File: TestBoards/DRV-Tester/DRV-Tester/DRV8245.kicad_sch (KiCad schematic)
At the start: 2 parts, among them IC1 DRV8245SQRXZRQ1, U1 PDRV8245HRXZQ1

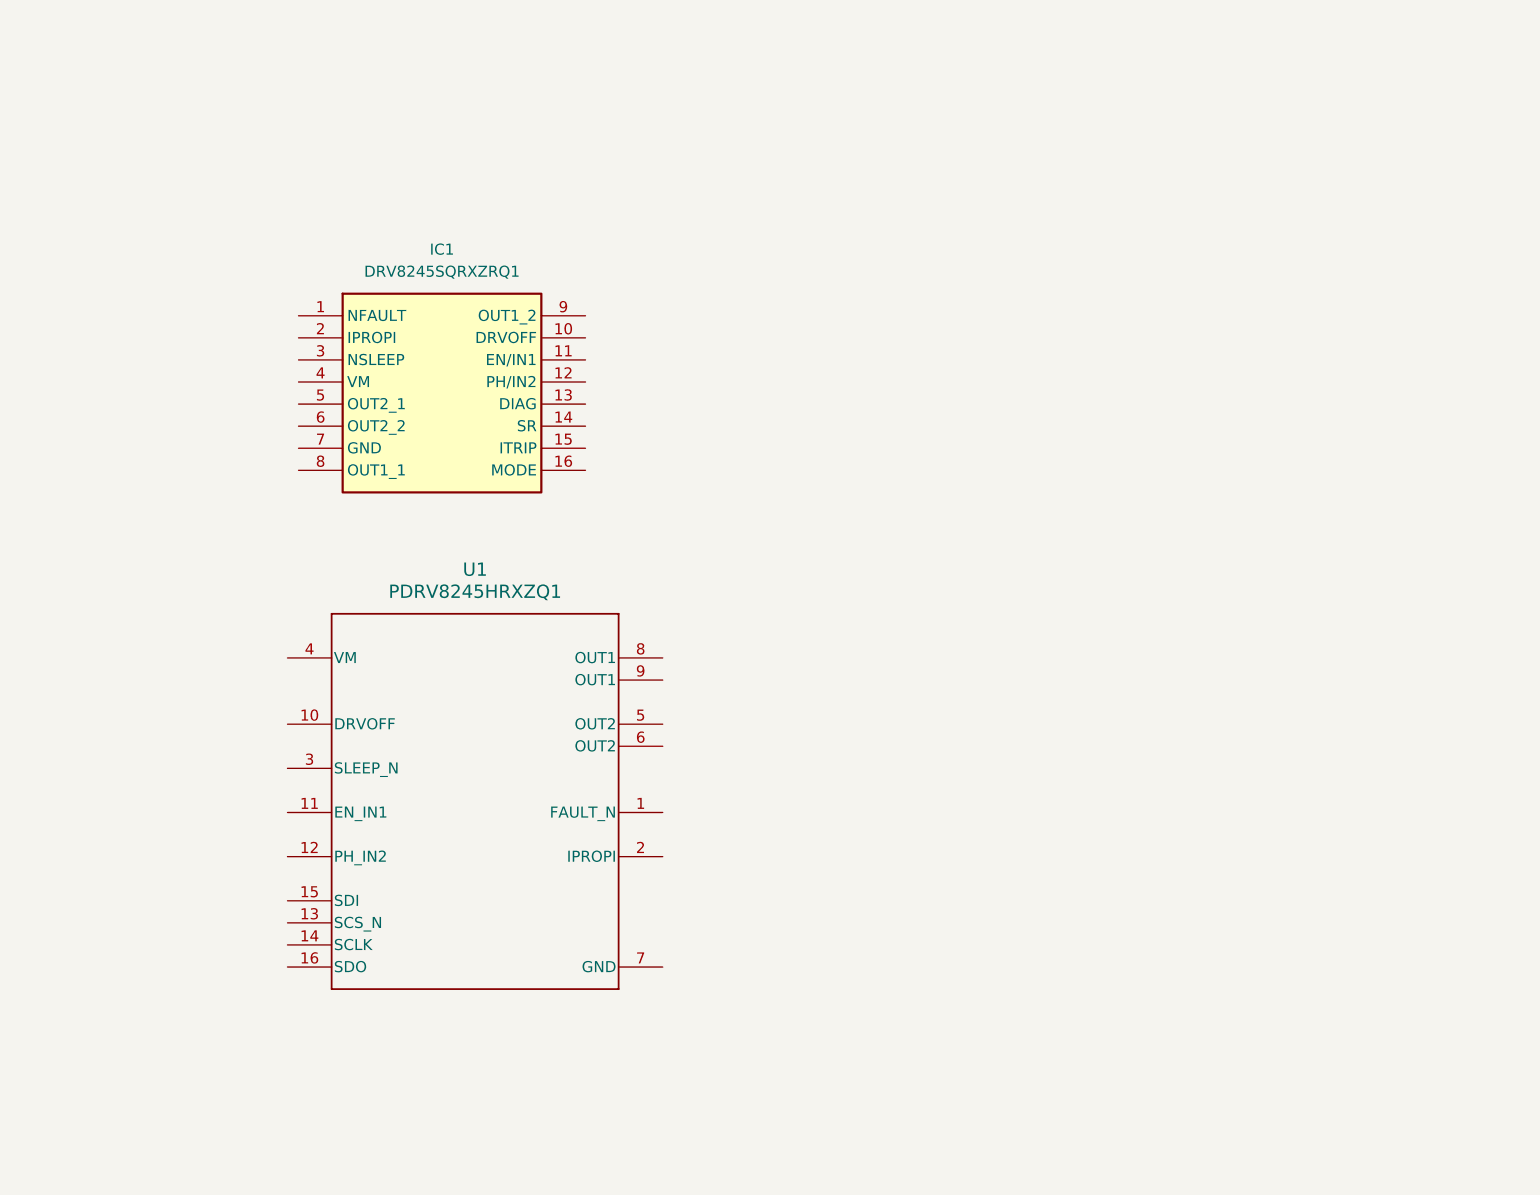
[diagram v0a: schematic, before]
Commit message: update new tester board sch
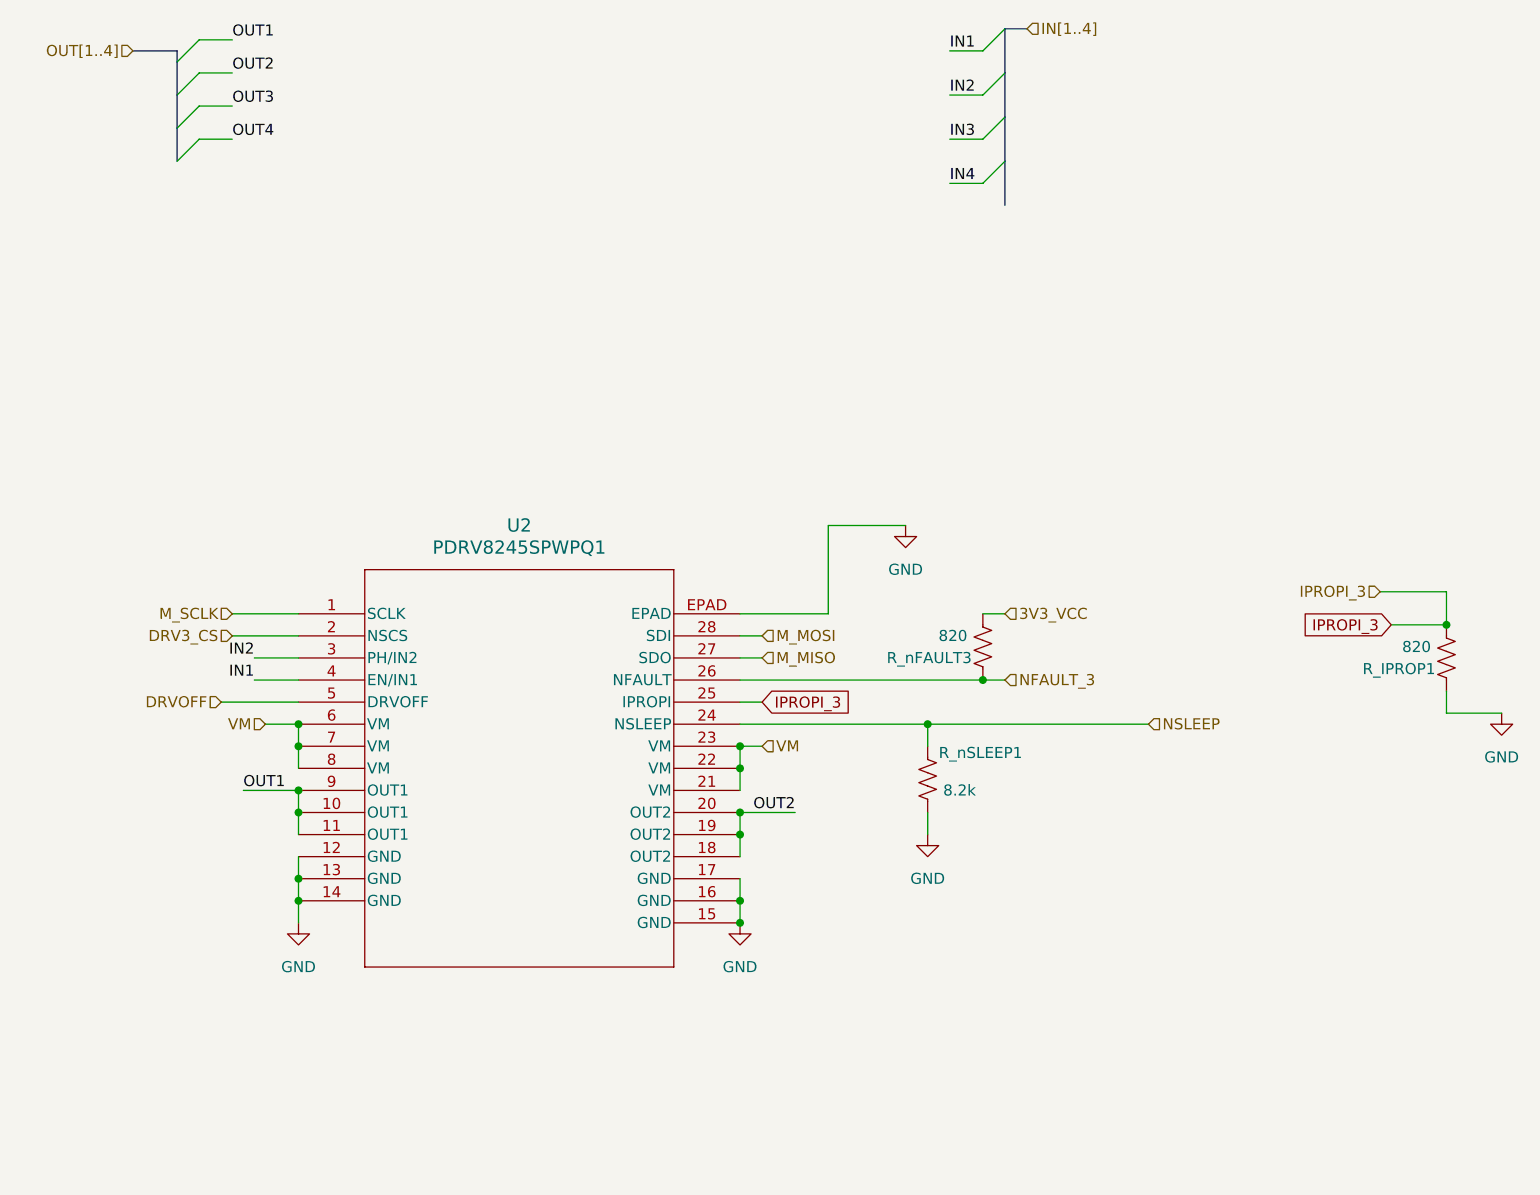
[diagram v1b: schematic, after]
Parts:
- removed IC1: DRV8245SQRXZRQ1, SamacSys_Parts:DRV8245HQRXZRQ1, symbol SamacSys_Parts:DRV8245SQRXZRQ1
- removed U1: PDRV8245HRXZQ1, PDRV8245SPWPQ1:U_PWP0028R_TEX, symbol PDRV8245HRXZQ1:PDRV8245HRXZQ1
- added R_IPROP1, R_nFAULT3: 820, Resistor_SMD:R_0603_1608Metric, symbol Device:R_US
- added R_nSLEEP1: 8.2k, Resistor_SMD:R_0603_1608Metric, symbol Device:R_US
- added U2: PDRV8245SPWPQ1, U_PWP0028R_TEX, symbol PDRV8245SPWPQ1:PDRV8245SPWPQ1
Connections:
- new net 3V3_VCC: R_nFAULT3.1
- new net DRV3_CS: U2.2 (NSCS)
- new net DRVOFF: U2.5 (DRVOFF)
- new net GND: R_IPROP1.2, R_nSLEEP1.1, U2.12 (GND), U2.13 (GND), U2.14 (GND), U2.15 (GND), U2.16 (GND), U2.17 (GND), U2.EPAD
- new net IN1: U2.4 (EN/IN1)
- new net IN2: U2.3 (PH/IN2)
- new net IPROPI_3: R_IPROP1.1, U2.25 (IPROPI)
- new net M_MISO: U2.27 (SDO)
- new net M_MOSI: U2.28 (SDI)
- new net M_SCLK: U2.1 (SCLK)
- new net NFAULT_3: R_nFAULT3.2, U2.26 (NFAULT)
- new net NSLEEP: R_nSLEEP1.2, U2.24 (NSLEEP)
- new net OUT1: U2.10 (OUT1), U2.11 (OUT1), U2.9 (OUT1)
- new net OUT2: U2.18 (OUT2), U2.19 (OUT2), U2.20 (OUT2)
- new net VM: U2.21 (VM), U2.22 (VM), U2.23 (VM), U2.6 (VM), U2.7 (VM), U2.8 (VM)

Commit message: update tester board with layout
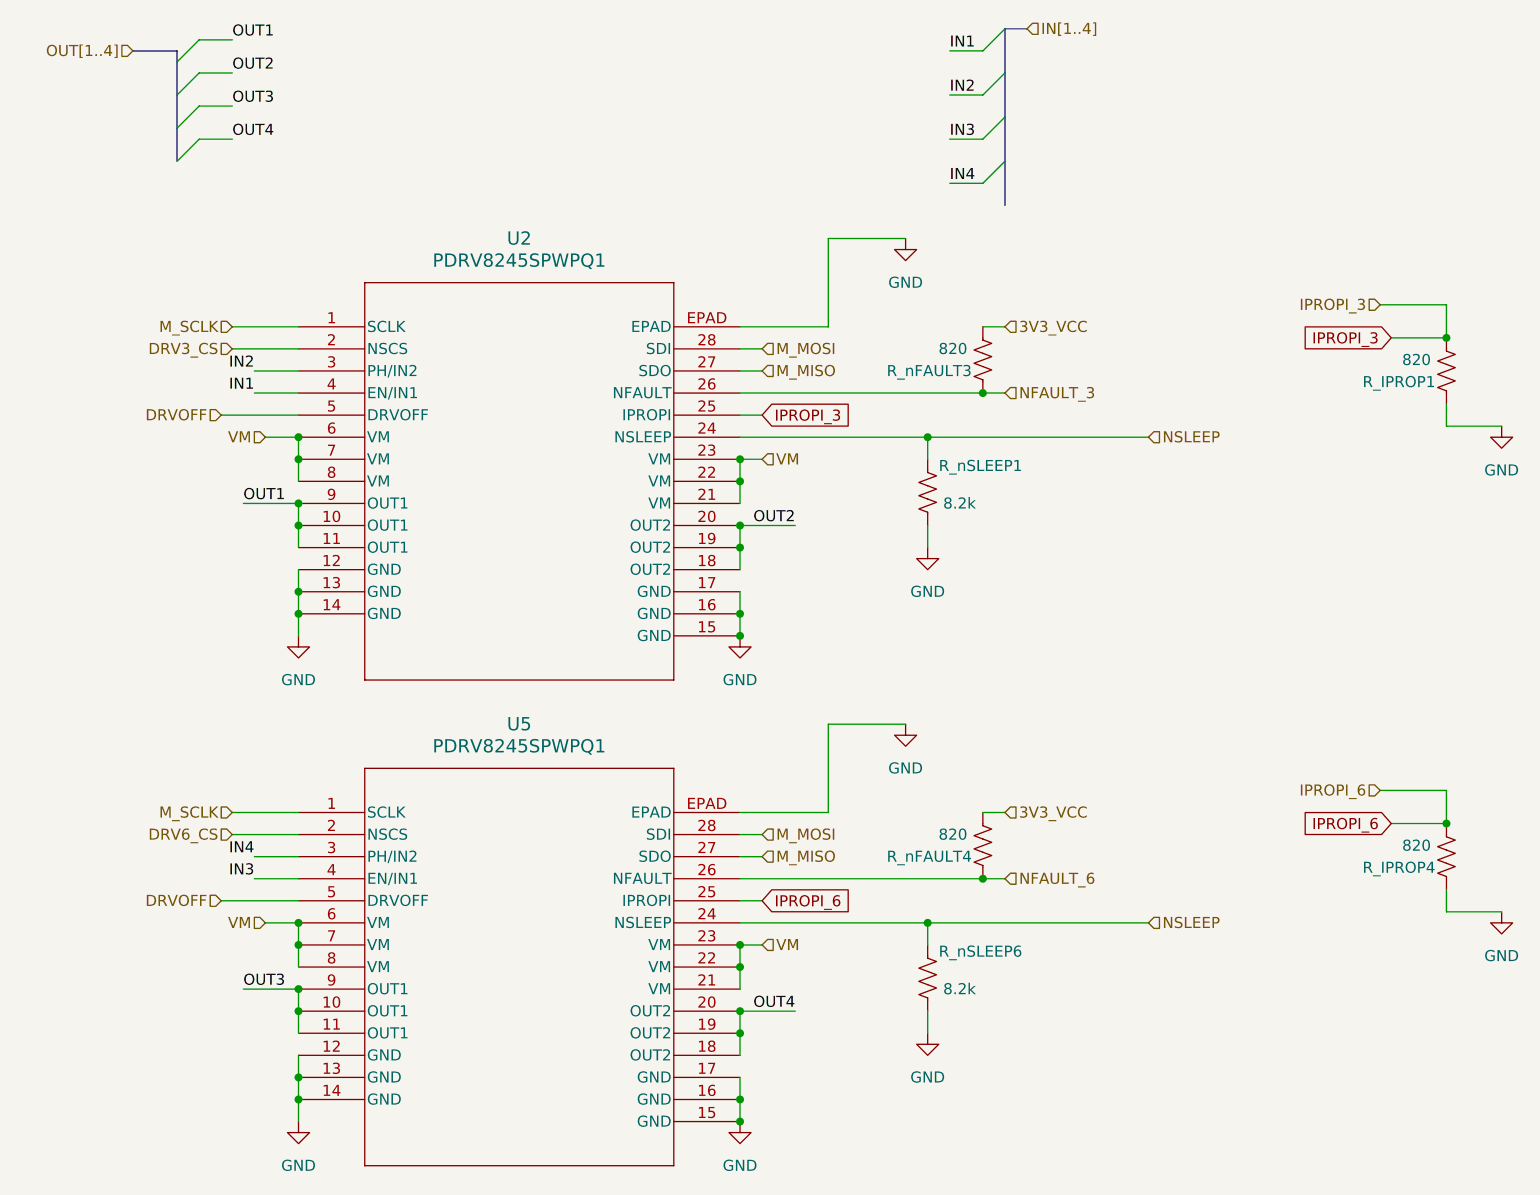
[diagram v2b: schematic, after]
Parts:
- added R_IPROP4, R_nFAULT4: 820, Resistor_SMD:R_0603_1608Metric, symbol Device:R_US
- added R_nSLEEP6: 8.2k, Resistor_SMD:R_0603_1608Metric, symbol Device:R_US
- added U5: PDRV8245SPWPQ1, U_PWP0028R_TEX, symbol PDRV8245SPWPQ1:PDRV8245SPWPQ1
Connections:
- net 3V3_VCC: now also R_nFAULT4.1
- net DRVOFF: now also U5.5 (DRVOFF)
- net GND: now also R_IPROP4.2, R_nSLEEP6.1, U5.12 (GND), U5.13 (GND), U5.14 (GND), U5.15 (GND), U5.16 (GND), U5.17 (GND), U5.EPAD
- net IN3: now also U5.4 (EN/IN1)
- net IN4: now also U5.3 (PH/IN2)
- net M_MISO: now also U5.27 (SDO)
- net M_MOSI: now also U5.28 (SDI)
- net M_SCLK: now also U5.1 (SCLK)
- net NSLEEP: now also R_nSLEEP6.2, U5.24 (NSLEEP)
- net OUT3: now also U5.10 (OUT1), U5.11 (OUT1), U5.9 (OUT1)
- net OUT4: now also U5.18 (OUT2), U5.19 (OUT2), U5.20 (OUT2)
- net VM: now also U5.21 (VM), U5.22 (VM), U5.23 (VM), U5.6 (VM), U5.7 (VM), U5.8 (VM)
- new net DRV6_CS: U5.2 (NSCS)
- new net IPROPI_6: R_IPROP4.1, U5.25 (IPROPI)
- new net NFAULT_6: R_nFAULT4.2, U5.26 (NFAULT)
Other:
- moved on the sheet: R_IPROP1, R_nFAULT3, R_nSLEEP1, U2
